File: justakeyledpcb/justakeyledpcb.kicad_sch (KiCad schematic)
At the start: 15 parts, among them SW1 SW_Push, SW2 SW_Push, SW3 SW_Push, SW4 SW_Push, U1 XIAO-RP2040-DIP

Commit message: Adding some stuff
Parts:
- added SW5: SW_Push, SW_PUSH_6mm, symbol Switch:SW_Push
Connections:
- net GND: now also SW5.2
- net Button Start: now reaches U1.7 (GPIO0/TX)
- net Button Start: now also SW5.1
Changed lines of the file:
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@@
+	(wire
+		(pts
+			(xy 97.79 93.98) (xy 102.87 93.98)
+		)
+		(stroke
+			(width 0)
+			(type default)
+		)
+	)
 	(wire
 		(pts
@@
 		)
 	)
+	(global_label "Button Start"
+		(shape input)
+		(at 68.58 55.88 180)
+		(fields_autoplaced yes)
+		(effects
+			(font
+				(size 1.27 1.27)
+			)
+			(justify right)
+		)
+		(property "Intersheetrefs" "${INTERSHEET_REFS}"
+			(at 53.8627 55.88 0)
+			(effects
+				(font
+					(size 1.27 1.27)
+				)
+				(justify right)
+				(hide yes)
+			)
+		)
+	)
 	(global_label "LED 1"
 		(shape input)
@@
 		(property "Intersheetrefs" "${INTERSHEET_REFS}"
 			(at 150.1406 45.72 0)
+			(effects
+				(font
+					(size 1.27 1.27)
+				)
+				(justify right)
+				(hide yes)
+			)
+		)
+	)
+	(global_label "Button Start"
+		(shape input)
+		(at 97.79 93.98 180)
+		(fields_autoplaced yes)
+		(effects
+			(font
+				(size 1.27 1.27)
+			)
+			(justify right)
+		)
+		(property "Intersheetrefs" "${INTERSHEET_REFS}"
+			(at 83.0727 93.98 0)
 			(effects
 				(font
@@
 	)
 	(symbol
+		(lib_id "Switch:SW_Push")
+		(at 73.66 55.88 0)
+		(unit 1)
+		(exclude_from_sim no)
+		(in_bom yes)
+		(on_board yes)
+		(dnp no)
+		(fields_autoplaced yes)
+		(property "Reference" "SW5"
+			(at 73.66 48.26 0)
+			(effects
+				(font
+					(size 1.27 1.27)
+				)
+			)
+		)
+		(property "Value" "SW_Push"
+			(at 73.66 50.8 0)
+			(effects
+				(font
+					(size 1.27 1.27)
+				)
+			)
+		)
+		(property "Footprint" "SW_PUSH_6mm"
+			(at 73.66 50.8 0)
+			(effects
+				(font
+					(size 1.27 1.27)
+				)
+				(hide yes)
+			)
+		)
+		(property "Datasheet" "~"
+			(at 73.66 50.8 0)
+			(effects
+				(font
+					(size 1.27 1.27)
+				)
+				(hide yes)
+			)
+		)
+		(property "Description" "Push button switch, generic, two pins"
+			(at 73.66 55.88 0)
+			(effects
+				(font
+					(size 1.27 1.27)
+				)
+				(hide yes)
+			)
+		)
+		(pin "1"
+		)
+		(pin "2"
+		)
+		(instances
+			(project ""
+				(path "/15b9dd11-e1bc-4be5-bc48-736a919b65d9"
+					(reference "SW5")
+					(unit 1)
+				)
+			)
+		)
+	)
+	(symbol
 		(lib_id "power:GND")
 		(at 179.07 72.39 0)
@@
 					(unit 1)
 				)
+			)
+		)
+	)
+	(symbol
+		(lib_id "power:GND")
+		(at 78.74 55.88 0)
+		(unit 1)
+		(exclude_from_sim no)
+		(in_bom yes)
+		(on_board yes)
+		(dnp no)
+		(fields_autoplaced yes)
+		(property "Reference" "#PWR011"
+			(at 78.74 62.23 0)
+			(effects
+				(font
+					(size 1.27 1.27)
+				)
+				(hide yes)
+			)
+		)
+		(property "Value" "GND"
+			(at 78.74 60.96 0)
+			(effects
+				(font
+					(size 1.27 1.27)
+				)
+			)
+		)
+		(property "Footprint" ""
+			(at 78.74 55.88 0)
+			(effects
+				(font
+					(size 1.27 1.27)
+				)
+				(hide yes)
+			)
+		)
+		(property "Datasheet" ""
+			(at 78.74 55.88 0)
+			(effects
+				(font
+					(size 1.27 1.27)
+				)
+				(hide yes)
+			)
+		)
+		(property "Description" "Power symbol creates a global label with name \"GND\" , ground"
+			(at 78.74 55.88 0)
+			(effects
+				(font
+					(size 1.27 1.27)
+				)
+				(hide yes)
+			)
+		)
+		(pin "1"
+		)
+		(instances
+			(project ""
+				(path "/15b9dd11-e1bc-4be5-bc48-736a919b65d9"
+					(reference "#PWR011")
+					(unit 1)
+				)

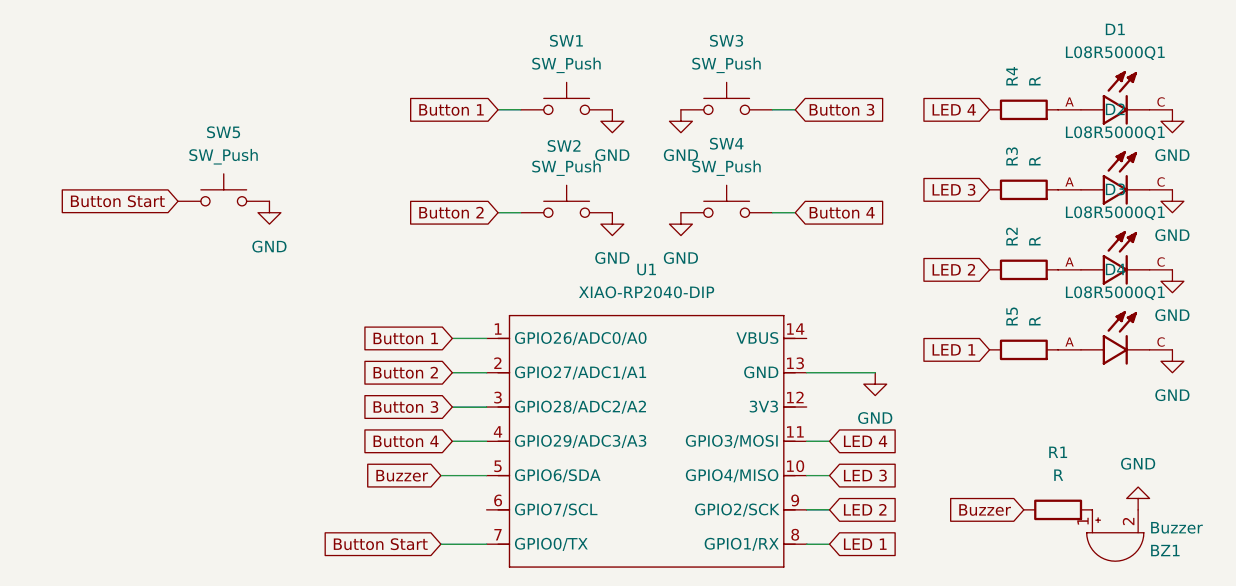
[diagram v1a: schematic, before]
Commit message: Cleared the A0 pin for ard seeding for random num and moved the pin downwards
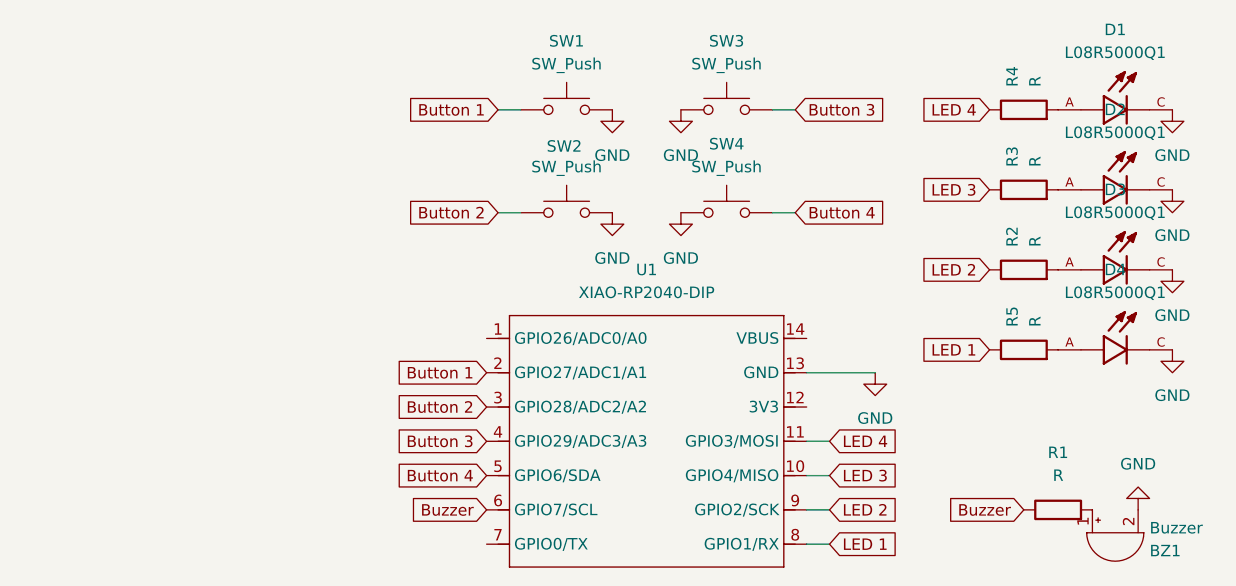
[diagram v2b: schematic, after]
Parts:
- removed SW5: SW_Push, SW_PUSH_6mm, symbol Switch:SW_Push
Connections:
- net Button 1: now also U1.2 (GPIO27/ADC1/A1); no longer U1.1 (GPIO26/ADC0/A0)
- net Button 2: now also U1.3 (GPIO28/ADC2/A2); no longer U1.2 (GPIO27/ADC1/A1)
- net Button 3: now also U1.4 (GPIO29/ADC3/A3); no longer U1.3 (GPIO28/ADC2/A2)
- net Button 4: now also U1.5 (GPIO6/SDA); no longer U1.4 (GPIO29/ADC3/A3)
- net Buzzer: now also U1.6 (GPIO7/SCL); no longer U1.5 (GPIO6/SDA)
- net Button Start: no longer names the net of U1.7 (GPIO0/TX)

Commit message: added the place for an external power source in the PCB schem and updated the PCB design
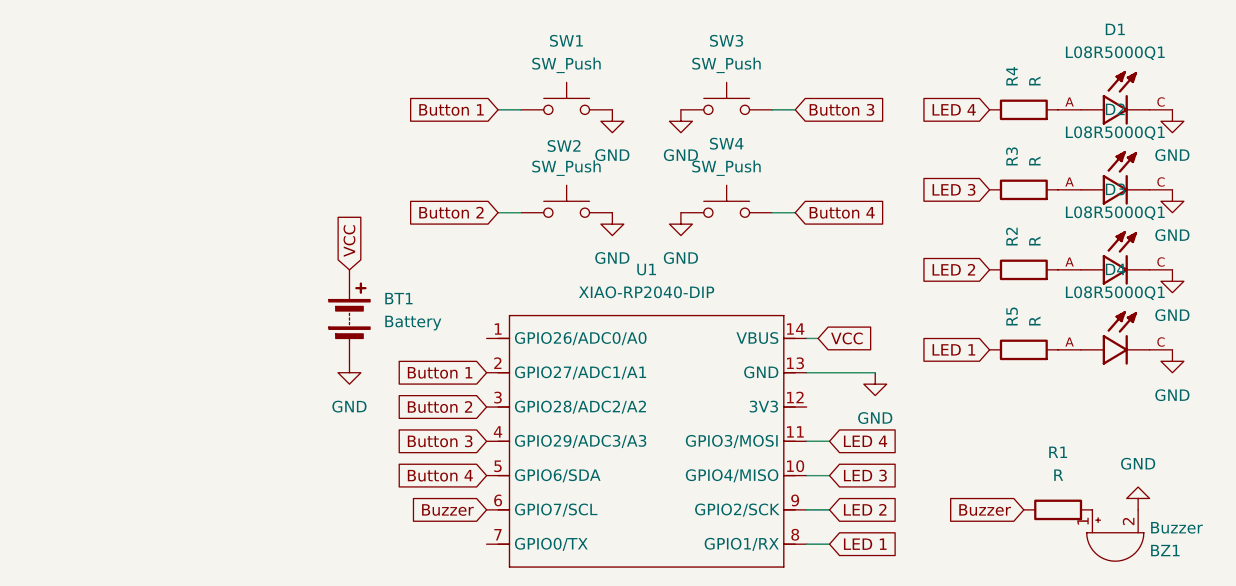
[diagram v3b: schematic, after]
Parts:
- added BT1: Battery, TestPoint:TestPoint_2Pads_Pitch2.54mm_Drill0.8mm, symbol Device:Battery
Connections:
- net GND: now also BT1.2 (-)
- net VCC: now reaches U1.14 (VBUS)
- net VCC: now also BT1.1 (+)
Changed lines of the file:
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@@
+	(wire
+		(pts
+			(xy 138.43 71.12) (xy 139.7 71.12)
+		)
+		(stroke
+			(width 0)
+			(type default)
+		)
+	)
 	(wire
 		(pts
@@
 		)
 	)
+	(global_label "VCC"
+		(shape input)
+		(at 139.7 71.12 0)
+		(fields_autoplaced yes)
+		(effects
+			(font
+				(size 1.27 1.27)
+			)
+			(justify left)
+		)
+		(property "Intersheetrefs" "${INTERSHEET_REFS}"
+			(at 146.3138 71.12 0)
+			(effects
+				(font
+					(size 1.27 1.27)
+				)
+				(justify left)
+				(hide yes)
+			)
+		)
+	)
 	(global_label "Button 2"
 		(shape input)
@@
 		)
 	)
+	(global_label "VCC"
+		(shape input)
+		(at 87.63 63.5 90)
+		(fields_autoplaced yes)
+		(effects
+			(font
+				(size 1.27 1.27)
+			)
+			(justify left)
+		)
+		(property "Intersheetrefs" "${INTERSHEET_REFS}"
+			(at 87.63 56.8862 90)
+			(effects
+				(font
+					(size 1.27 1.27)
+				)
+				(justify left)
+				(hide yes)
+			)
+		)
+	)
 	(global_label "Button 1"
 		(shape input)
@@
 				(justify right)
 				(hide yes)
+			)
+		)
+	)
+	(symbol
+		(lib_id "Device:Battery")
+		(at 87.63 68.58 0)
+		(unit 1)
+		(exclude_from_sim no)
+		(in_bom yes)
+		(on_board yes)
+		(dnp no)
+		(fields_autoplaced yes)
+		(property "Reference" "BT1"
+			(at 91.44 66.7384 0)
+			(effects
+				(font
+					(size 1.27 1.27)
+				)
+				(justify left)
+			)
+		)
+		(property "Value" "Battery"
+			(at 91.44 69.2784 0)
+			(effects
+				(font
+					(size 1.27 1.27)
+				)
+				(justify left)
+			)
+		)
+		(property "Footprint" "TestPoint:TestPoint_2Pads_Pitch2.54mm_Drill0.8mm"
+			(at 87.63 67.056 90)
+			(effects
+				(font
+					(size 1.27 1.27)
+				)
+				(hide yes)
+			)
+		)
+		(property "Datasheet" "~"
+			(at 87.63 67.056 90)
+			(effects
+				(font
+					(size 1.27 1.27)
+				)
+				(hide yes)
+			)
+		)
+		(property "Description" "Multiple-cell battery"
+			(at 87.63 68.58 0)
+			(effects
+				(font
+					(size 1.27 1.27)
+				)
+				(hide yes)
+			)
+		)
+		(pin "1"
+		)
+		(pin "2"
+		)
+		(instances
+			(project ""
+				(path "/15b9dd11-e1bc-4be5-bc48-736a919b65d9"
+					(reference "BT1")
+					(unit 1)
+				)
 			)
 		)
@@
 					(unit 1)
 				)
+			)
+		)
+	)
+	(symbol
+		(lib_id "power:GND")
+		(at 87.63 73.66 0)
+		(unit 1)
+		(exclude_from_sim no)
+		(in_bom yes)
+		(on_board yes)
+		(dnp no)
+		(fields_autoplaced yes)
+		(property "Reference" "#PWR011"
+			(at 87.63 80.01 0)
+			(effects
+				(font
+					(size 1.27 1.27)
+				)
+				(hide yes)
+			)
+		)
+		(property "Value" "GND"
+			(at 87.63 78.74 0)
+			(effects
+				(font
+					(size 1.27 1.27)
+				)
+			)
+		)
+		(property "Footprint" ""
+			(at 87.63 73.66 0)
+			(effects
+				(font
+					(size 1.27 1.27)
+				)
+				(hide yes)
+			)
+		)
+		(property "Datasheet" ""
+			(at 87.63 73.66 0)
+			(effects
+				(font
+					(size 1.27 1.27)
+				)
+				(hide yes)
+			)
+		)
+		(property "Description" "Power symbol creates a global label with name \"GND\" , ground"
+			(at 87.63 73.66 0)
+			(effects
+				(font
+					(size 1.27 1.27)
+				)
+				(hide yes)
+			)
+		)
+		(pin "1"
+		)
+		(instances
+			(project ""
+				(path "/15b9dd11-e1bc-4be5-bc48-736a919b65d9"
+					(reference "#PWR011")
+					(unit 1)
+				)
